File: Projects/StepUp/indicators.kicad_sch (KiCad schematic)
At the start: 10 parts, among them Q7 2N7002-7-F

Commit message: feat(v0.2): Release, PCBs ordered!
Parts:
- removed D14: LED_ARGB, LED_THT:LED_D5.0mm-4_RGB, symbol Device:LED_ARGB
- added D15: LED_ARGB, LED_THT:LED_D5.0mm-4_RGB_Staggered_Pins, symbol Device:LED_ARGB
- BZ1: MPN (none) -> PS1240P02CT3; Manufacturer (none) -> TDK Corporation; now in the parts list
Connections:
- net +3V3: now also D15.1 (A)
- net at R49.1: now also D15.2 (RK)
- net at R50.1: now also D15.3 (GK)
- net at R51.1: now also D15.4 (BK)
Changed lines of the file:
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@@
+			)
+		)
+		(property "MANUFACTURER" ""
+			(at 187.96 113.03 0)
+			(effects
+				(font
+					(size 1.27 1.27)
+				)
+				(hide yes)
 			)
 		)
@@
 		(on_board yes)
 		(dnp no)
-		(property "Reference" "#PWR094"
+		(property "Reference" "#PWR091"
 			(at 191.77 82.55 0)
 			(effects
@@
 			(project "StepUp"
 				(path "/e0cca1c7-c263-49eb-8c40-74000ebe5285/9dda156e-3fdf-45bb-95f8-ac79c3ca0e44"
-					(reference "#PWR094")
+					(reference "#PWR091")
+					(unit 1)
+				)
+			)
+		)
+	)
+	(symbol
+		(lib_id "Device:LED_ARGB")
+		(at 97.79 107.95 0)
+		(unit 1)
+		(exclude_from_sim no)
+		(in_bom yes)
+		(on_board yes)
+		(dnp no)
+		(fields_autoplaced yes)
+		(property "Reference" "D15"
+			(at 97.79 93.98 0)
+			(effects
+				(font
+					(size 1.27 1.27)
+				)
+			)
+		)
+		(property "Value" "LED_ARGB"
+			(at 97.79 96.52 0)
+			(effects
+				(font
+					(size 1.27 1.27)
+				)
+			)
+		)
+		(property "Footprint" "LED_THT:LED_D5.0mm-4_RGB_Staggered_Pins"
+			(at 97.79 109.22 0)
+			(effects
+				(font
+					(size 1.27 1.27)
+				)
+				(hide yes)
+			)
+		)
+		(property "Datasheet" "~"
+			(at 97.79 109.22 0)
+			(effects
+				(font
+					(size 1.27 1.27)
+				)
+				(hide yes)
+			)
+		)
+		(property "Description" "RGB LED, anode/red/green/blue"
+			(at 97.79 107.95 0)
+			(effects
+				(font
+					(size 1.27 1.27)
+				)
+				(hide yes)
+			)
+		)
+		(property "MANUFACTURER" ""
+			(at 97.79 107.95 0)
+			(effects
+				(font
+					(size 1.27 1.27)
+				)
+				(hide yes)
+			)
+		)
+		(pin "3"
+		)
+		(pin "1"
+		)
+		(pin "4"
+		)
+		(pin "2"
+		)
+		(instances
+			(project ""
+				(path "/e0cca1c7-c263-49eb-8c40-74000ebe5285/9dda156e-3fdf-45bb-95f8-ac79c3ca0e44"
+					(reference "D15")
 					(unit 1)
 				)
@@
 			)
 		)
+		(property "MANUFACTURER" ""
+			(at 200.66 104.14 0)
+			(effects
+				(font
+					(size 1.27 1.27)
+				)
+				(hide yes)
+			)
+		)
 		(pin "2"
 		)
@@
 		(unit 1)
 		(exclude_from_sim no)
-		(in_bom no)
+		(in_bom yes)
 		(on_board yes)
 		(dnp no)
@@
 		)
 		(property "SnapEDA_Link" ""
+			(at 218.44 87.63 0)
+			(effects
+				(font
+					(size 1.27 1.27)
+				)
+				(hide yes)
+			)
+		)
+		(property "MANUFACTURER" ""
+			(at 218.44 87.63 0)
+			(effects
+				(font
+					(size 1.27 1.27)
+				)
+				(hide yes)
+			)
+		)
+		(property "MPN" "PS1240P02CT3"
+			(at 218.44 87.63 0)
+			(effects
+				(font
+					(size 1.27 1.27)
+				)
+				(hide yes)
+			)
+		)
+		(property "Manufacturer" "TDK Corporation"
 			(at 218.44 87.63 0)
 			(effects
@@
 			)
 		)
+		(property "MANUFACTURER" ""
+			(at 77.47 102.87 0)
+			(effects
+				(font
+					(size 1.27 1.27)
+				)
+				(hide yes)
+			)
+		)
 		(pin "1"
 		)
@@
 			)
 		)
+		(property "MANUFACTURER" ""
+			(at 77.47 107.95 0)
+			(effects
+				(font
+					(size 1.27 1.27)
+				)
+				(hide yes)
+			)
+		)
 		(pin "1"
 		)
@@
 			)
 		)
+		(property "MANUFACTURER" ""
+			(at 200.66 88.9 0)
+			(effects
+				(font
+					(size 1.27 1.27)
+				)
+				(hide yes)
+			)
+		)
 		(pin "1"
 		)
@@
 			)
 		)
+		(property "MANUFACTURER" ""
+			(at 200.66 80.01 0)
+			(effects
+				(font
+					(size 1.27 1.27)
+				)
+				(hide yes)
+			)
+		)
 		(pin "1"
 		)
@@
 			)
 		)
+		(property "MANUFACTURER" ""
+			(at 181.61 106.68 0)
+			(effects
+				(font
+					(size 1.27 1.27)
+				)
+				(hide yes)
+			)
+		)
 		(pin "1"
 		)
@@
 		(on_board yes)
 		(dnp no)
-		(property "Reference" "#PWR093"
+		(property "Reference" "#PWR090"
 			(at 187.96 125.73 0)
 			(effects
@@
 			(project "StepUp"
 				(path "/e0cca1c7-c263-49eb-8c40-74000ebe5285/9dda156e-3fdf-45bb-95f8-ac79c3ca0e44"
-					(reference "#PWR093")
-					(unit 1)
-				)
-			)
-		)
-	)
-	(symbol
-		(lib_id "Device:LED_ARGB")
-		(at 97.79 107.95 0)
-		(unit 1)
-		(exclude_from_sim no)
-		(in_bom no)
-		(on_board yes)
-		(dnp no)
-		(fields_autoplaced yes)
-		(property "Reference" "D14"
-			(at 97.79 93.98 0)
-			(effects
-				(font
-					(size 1.27 1.27)
-				)
-			)
-		)
-		(property "Value" "LED_ARGB"
-			(at 97.79 96.52 0)
-			(effects
-				(font
-					(size 1.27 1.27)
-				)
-			)
-		)
-		(property "Footprint" "LED_THT:LED_D5.0mm-4_RGB"
-			(at 97.79 109.22 0)
-			(effects
-				(font
-					(size 1.27 1.27)
-				)
-				(hide yes)
-			)
-		)
-		(property "Datasheet" "~"
-			(at 97.79 109.22 0)
-			(effects
-				(font
-					(size 1.27 1.27)
-				)
-				(hide yes)
-			)
-		)
-		(property "Description" "RGB LED, anode/red/green/blue"
-			(at 97.79 107.95 0)
-			(effects
-				(font
-					(size 1.27 1.27)
-				)
-				(hide yes)
-			)
-		)
-		(pin "1"
-		)
-		(pin "4"
-		)
-		(pin "3"
-		)
-		(pin "2"
-		)
-		(instances
-			(project ""
-				(path "/e0cca1c7-c263-49eb-8c40-74000ebe5285/9dda156e-3fdf-45bb-95f8-ac79c3ca0e44"
-					(reference "D14")
+					(reference "#PWR090")
 					(unit 1)
 				)
@@
 		(on_board yes)
 		(dnp no)
-		(property "Reference" "#PWR095"
+		(property "Reference" "#PWR092"
 			(at 200.66 125.73 0)
 			(effects
@@
 			(project "StepUp"
 				(path "/e0cca1c7-c263-49eb-8c40-74000ebe5285/9dda156e-3fdf-45bb-95f8-ac79c3ca0e44"
-					(reference "#PWR095")
+					(reference "#PWR092")
 					(unit 1)
 				)
@@
 		(on_board yes)
 		(dnp no)
-		(property "Reference" "#PWR096"
+		(property "Reference" "#PWR093"
 			(at 209.55 82.55 0)
 			(effects
@@
 			(project "StepUp"
 				(path "/e0cca1c7-c263-49eb-8c40-74000ebe5285/9dda156e-3fdf-45bb-95f8-ac79c3ca0e44"
-					(reference "#PWR096")
+					(reference "#PWR093")
 					(unit 1)
 				)
@@
 		(on_board yes)
 		(dnp no)
-		(property "Reference" "#PWR092"
+		(property "Reference" "#PWR089"
 			(at 110.49 105.41 0)
 			(effects
@@
 			(project "StepUp"
 				(path "/e0cca1c7-c263-49eb-8c40-74000ebe5285/9dda156e-3fdf-45bb-95f8-ac79c3ca0e44"
-					(reference "#PWR092")
+					(reference "#PWR089")
 					(unit 1)
 				)
@@
 			(at 77.47 113.03 0)
 			(effects
+				(font
+					(size 1.27 1.27)
+				)
+				(hide yes)
+			)
+		)
+		(property "MANUFACTURER" ""
+			(at 77.47 113.03 0)
+			(effects

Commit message: feat(v0.3): Begin work on next rev
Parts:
- removed D15: LED_ARGB, LED_THT:LED_D5.0mm-4_RGB_Staggered_Pins, symbol Device:LED_ARGB
- removed JP2: SolderJumper_3_Bridged12, Jumper:SolderJumper-3_P1.3mm_Bridged12_RoundedPad1.0x1.5mm, symbol Jumper:SolderJumper_3_Bridged12
- added LED1: MP008267, Samacsys:MP008267, symbol Samacsys:MP008267
- added R56: 120R, Resistor_SMD:R_0603_1608Metric, symbol Device:R
- R50: renamed from R49; value 100R -> 120R; MPN RC0603FR-07100RL -> RC0603FR-07120RL
- R51: value 100R -> 120R; MPN RC0603FR-07100RL -> RC0603FR-07120RL
- R52: renamed from R50; value 100R -> 22R; MPN RC0603FR-07100RL -> RC0603FR-0722RL
- renumbered R52 to R53, R53 to R54, R54 to R55
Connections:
- net GND: now also LED1.2
- net VMotor: now also BZ1.2, R55.2
- net at R50.1: now also LED1.1
- net at R52.1: now also LED1.3
- net at R51.1: now also LED1.4, R56.1
- net MCU_LED_STATUS_1 renamed MCU_LED_RED
- net MCU_LED_STATUS_3 renamed MCU_LED_GREEN
- net MCU_LED_GREEN: now also R56.2
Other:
- note added: "LED BLUE"
- note added: "LED GREEN"
- note added: "LED RED"
- note added: "LED resistor calculations (matching mcd values)"
- note added: "RED - 20mA = 600 mcd → 1mA = 30mcd - 300mcd = 10mA - Vf=2V (typ), 3.3-2V = 1.3V/10mA = 130R → 120R BLUE - 20mA = 300 mcd → 1mA = 15 mcd - 300mcd = 20mA - Vf=3V (typ), 3.3-3V = 0.3V/20mA = 15R → 22R GREEN - 20mA = 1300 mcd → 1mA = 65 mcd - 300mcd = 4.6mA - Vf=3V (typ), 3.3-3V = 0.3V/4.6mA = 65R → 60R"
- note added: "Status LEDs, RGB 3-in-1, through-hole, clear dome"
- note added: "To indicate device states, f = 4kHz ~10V from the boost converter also used for the buzzer"
- note removed: "LED power calculations (TBD)"
- note removed: "Status LEDs, surface-mount, side-entry, clear"
- note removed: "To indicate device states, f = 4kHz User selectable voltage, 3v3 or 10V for motor (default = 3v3)"
- note removed: "Vf_red = ...V Vf_green = ...V Vf_blue = ...V"
- moved on the sheet: R50, R52

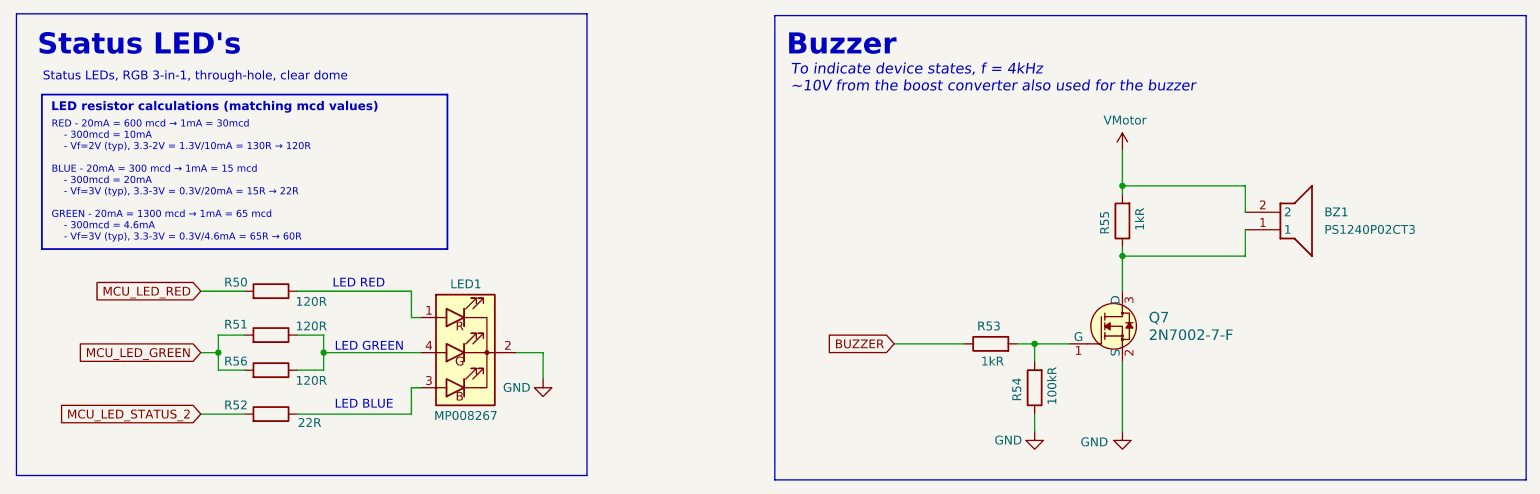
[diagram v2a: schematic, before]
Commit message: feat(v0.3): Boost layout complete
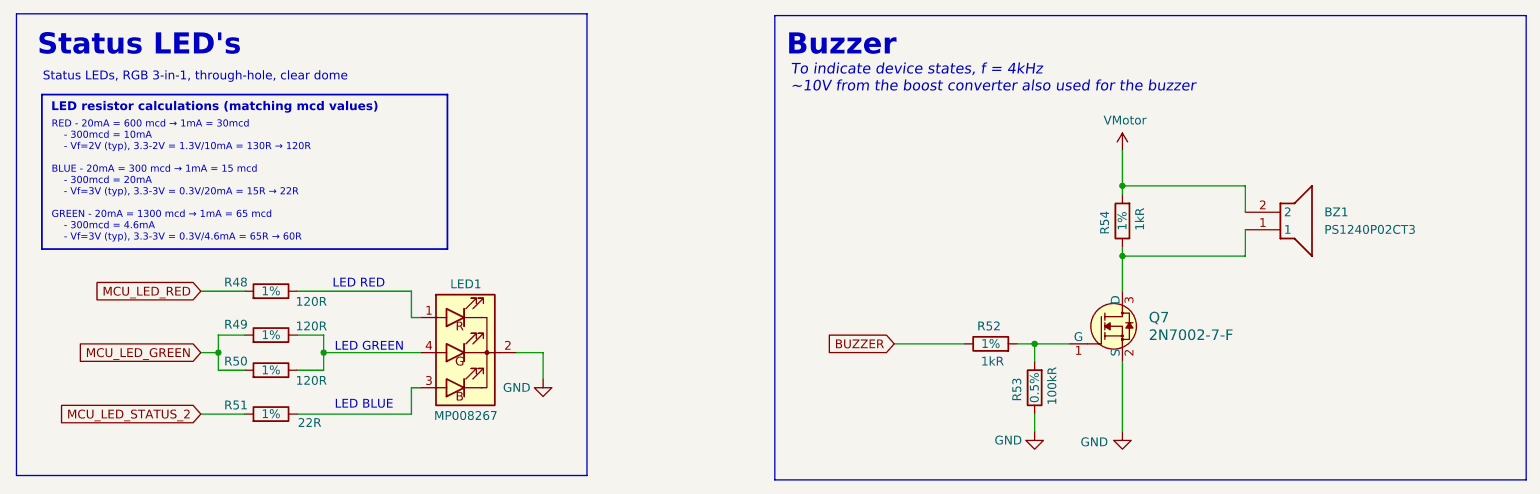
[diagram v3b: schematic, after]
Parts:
- renumbered R50 to R48, R51 to R49, R56 to R50, R52 to R51, R53 to R52, R54 to R53, R55 to R54
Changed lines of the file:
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@@
 		(on_board yes)
 		(dnp no)
-		(property "Reference" "R54"
+		(property "Reference" "R53"
 			(at 185.42 113.284 90)
 			(effects
@@
 		)
 		(property "Tolerance" "0.5%"
-			(at 187.96 113.03 0)
-			(effects
-				(font
-					(size 1.27 1.27)
-				)
-				(hide yes)
+			(at 187.96 113.03 90)
+			(effects
+				(font
+					(size 1.27 1.27)
+				)
 			)
 		)
@@
 			(project "StepUp"
 				(path "/e0cca1c7-c263-49eb-8c40-74000ebe5285/9dda156e-3fdf-45bb-95f8-ac79c3ca0e44"
-					(reference "R54")
+					(reference "R53")
 					(unit 1)
 				)
@@
 		(on_board yes)
 		(dnp no)
-		(property "Reference" "R50"
+		(property "Reference" "R48"
 			(at 72.39 97.79 90)
 			(effects
@@
 		)
 		(property "Tolerance" "1%"
-			(at 77.47 99.06 0)
-			(effects
-				(font
-					(size 1.27 1.27)
-				)
-				(hide yes)
+			(at 77.47 99.06 90)
+			(effects
+				(font
+					(size 1.27 1.27)
+				)
 			)
 		)
@@
 			(project "StepUp"
 				(path "/e0cca1c7-c263-49eb-8c40-74000ebe5285/9dda156e-3fdf-45bb-95f8-ac79c3ca0e44"
-					(reference "R50")
+					(reference "R48")
 					(unit 1)
 				)
@@
 		(on_board yes)
 		(dnp no)
-		(property "Reference" "R52"
+		(property "Reference" "R51"
 			(at 72.39 115.57 90)
 			(effects
@@
 		)
 		(property "Tolerance" "1%"
-			(at 77.47 116.84 0)
-			(effects
-				(font
-					(size 1.27 1.27)
-				)
-				(hide yes)
+			(at 77.47 116.84 90)
+			(effects
+				(font
+					(size 1.27 1.27)
+				)
 			)
 		)
@@
 			(project "StepUp"
 				(path "/e0cca1c7-c263-49eb-8c40-74000ebe5285/9dda156e-3fdf-45bb-95f8-ac79c3ca0e44"
-					(reference "R52")
+					(reference "R51")
 					(unit 1)
 				)
@@
 		(on_board yes)
 		(dnp no)
-		(property "Reference" "R55"
+		(property "Reference" "R54"
 			(at 198.12 89.154 90)
 			(effects
@@
 		)
 		(property "Tolerance" "1%"
-			(at 200.66 88.9 0)
-			(effects
-				(font
-					(size 1.27 1.27)
-				)
-				(hide yes)
+			(at 200.66 88.9 90)
+			(effects
+				(font
+					(size 1.27 1.27)
+				)
 			)
 		)
@@
 			(project "StepUp"
 				(path "/e0cca1c7-c263-49eb-8c40-74000ebe5285/9dda156e-3fdf-45bb-95f8-ac79c3ca0e44"
-					(reference "R55")
+					(reference "R54")
 					(unit 1)
 				)
@@
 		(on_board yes)
 		(dnp no)
-		(property "Reference" "R53"
+		(property "Reference" "R52"
 			(at 181.356 104.14 90)
 			(effects
@@
 		)
 		(property "Tolerance" "1%"
-			(at 181.61 106.68 0)
-			(effects
-				(font
-					(size 1.27 1.27)
-				)
-				(hide yes)
+			(at 181.61 106.68 90)
+			(effects
+				(font
+					(size 1.27 1.27)
+				)
 			)
 		)
@@
 			(project "StepUp"
 				(path "/e0cca1c7-c263-49eb-8c40-74000ebe5285/9dda156e-3fdf-45bb-95f8-ac79c3ca0e44"
-					(reference "R53")
+					(reference "R52")
 					(unit 1)
 				)
@@
 		(on_board yes)
 		(dnp no)
-		(property "Reference" "R51"
+		(property "Reference" "R49"
 			(at 72.39 103.886 90)
 			(effects
@@
 		)
 		(property "Tolerance" "1%"
-			(at 77.47 105.41 0)
-			(effects
-				(font
-					(size 1.27 1.27)
-				)
-				(hide yes)
+			(at 77.47 105.41 90)
+			(effects
+				(font
+					(size 1.27 1.27)
+				)
 			)
 		)
@@
 			(project "StepUp"
 				(path "/e0cca1c7-c263-49eb-8c40-74000ebe5285/9dda156e-3fdf-45bb-95f8-ac79c3ca0e44"
-					(reference "R51")
+					(reference "R49")
 					(unit 1)
 				)
@@
 		(on_board yes)
 		(dnp no)
-		(property "Reference" "R56"
+		(property "Reference" "R50"
 			(at 72.39 109.22 90)
 			(effects
@@
 		)
 		(property "Tolerance" "1%"
-			(at 77.47 110.49 0)
-			(effects
-				(font
-					(size 1.27 1.27)
-				)
-				(hide yes)
+			(at 77.47 110.49 90)
+			(effects
+				(font
+					(size 1.27 1.27)
+				)
 			)
 		)
@@
 			(project "StepUp"
 				(path "/e0cca1c7-c263-49eb-8c40-74000ebe5285/9dda156e-3fdf-45bb-95f8-ac79c3ca0e44"
-					(reference "R56")
+					(reference "R50")
 					(unit 1)
 				)

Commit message: feat(v0.3): Layout 90% complete
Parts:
- renumbered LED1 to LED2
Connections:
- net MCU_LED_STATUS_2 renamed MCU_LED_BLUE
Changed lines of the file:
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@@
 		)
 	)
-	(global_label "MCU_LED_STATUS_2"
+	(global_label "MCU_LED_BLUE"
 		(shape input)
 		(at 67.31 116.84 180)
@@
 		)
 		(property "Intersheetrefs" "${INTERSHEET_REFS}"
-			(at 45.9402 116.84 0)
+			(at 50.113 116.84 0)
 			(effects
 				(font
@@
 		(on_board yes)
 		(dnp no)
-		(property "Reference" "LED1"
+		(property "Reference" "LED2"
 			(at 105.664 98.044 0)
 			(effects
@@
 			(project ""
 				(path "/e0cca1c7-c263-49eb-8c40-74000ebe5285/9dda156e-3fdf-45bb-95f8-ac79c3ca0e44"
-					(reference "LED1")
+					(reference "LED2")
 					(unit 1)
 				)
